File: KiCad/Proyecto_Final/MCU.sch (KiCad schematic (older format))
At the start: 74 parts

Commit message: Esquematico terminado con test points.
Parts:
- added J?: 5v, symbol Connector_Generic:Conn_01x02
- added J?: I2C1, symbol Connector_Generic:Conn_01x02
- added TP? (x34): TestPoint, symbol Connector:TestPoint
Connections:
- net +3.3VA: now also TP?.1
- net +3V3: now also TP?.1
- net ADC_22MHz: now also TP?.1
- net ADC_45MHz: now also TP?.1
- net Filt_Bypass: now also TP?.1
- net Filtro: now also TP?.1
- net GND: now also J?.2 (Pin_2), TP?.1
- net I2C1_SCL: now also J?.1 (Pin_1), TP?.1
- net I2C1_SDA: now also J?.2 (Pin_2), TP?.1
- net MCU_CLK: now also TP?.1
- net MIX_CLK: now also TP?.1
- net NRST: now also TP?.1
- net RXHP: now also TP?.1
- net Rx_Amp: now also TP?.1
- net Rx_Amp_Bypass: now also TP?.1
- net Rx_Amp_Pwr: now also TP?.1
- net Rx_Mix: now also TP?.1
- net Rx_Mix_Bypass: now also TP?.1
- net SPI1_CS0: now also TP?.1
- net SPI1_CS1: now also TP?.1
- net SPI1_MISO: now also TP?.1
- net SPI1_MOSI: now also TP?.1
- net SPI1_SCK: now also TP?.1
- net SPI4_CS: now also TP?.1
- net SPI4_MISO: now also TP?.1
- net SPI4_MOSI: now also TP?.1
- net SPI4_SCK: now also TP?.1
- net SWCLK: now also TP?.1
- net SWDIO: now also TP?.1
- net SWO: now also TP?.1
- net Trx_CLK: now also TP?.1
- net Trx_Enable: now also TP?.1
- net Trx_Rx_Enable: now also TP?.1
- net VBUS: now also J?.1 (Pin_1), TP?.1

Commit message: Primer hito presentado y visado.
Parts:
- FB?: value 220 @ 100MHz -> 120 @ 100MHz
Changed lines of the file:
@@
 P 1250 1300
 F 0 "FB?" V 976 1300 50  0000 C CNN
-F 1 "220 @ 100MHz" V 1067 1300 50  0000 C CNN
+F 1 "120 @ 100MHz" V 1067 1300 50  0000 C CNN
 F 2 "" V 1180 1300 50  0001 C CNN
 F 3 "~" H 1250 1300 50  0001 C CNN

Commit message: Empezando con el pcb, loquita.
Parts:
- C100, C101, C110, C89, C90, C94, C96, C99: renamed from C?; footprint (none) -> Capacitor_SMD:C_0805_2012Metric
- C102, C104, C105, C106, C107, C108, C109, C111, C76, C77, C78, C79, C80, C81, C82, C83, C84, C85, C86, C87, C88, C93, C95, C97, C98: renamed from C?; footprint (none) -> Capacitor_SMD:C_0402_1005Metric
- C103, C91, C92: renamed from C?; footprint (none) -> Capacitor_SMD:CP_Elec_4x5.4
- D2: renamed from D?; footprint (none) -> LED_SMD:LED_0603_1608Metric
- FB1, FB2, FB3: renamed from FB?; footprint (none) -> Inductor_SMD:L_0402_1005Metric
- J10, J8: renamed from J?; footprint (none) -> Connector_PinHeader_2.54mm:PinHeader_2x03_P2.54mm_Vertical_SMD
- J11, J12, J16: renamed from J?; footprint (none) -> Connector_PinHeader_2.54mm:PinHeader_2x04_P2.54mm_Vertical_SMD
- J13, J9: renamed from J?; footprint (none) -> Connector_PinHeader_2.54mm:PinHeader_2x06_P2.54mm_Vertical_SMD
- J14: renamed from J?; footprint (none) -> Connector_PinHeader_2.54mm:PinHeader_2x08_P2.54mm_Vertical_SMD
- J15: renamed from J?; footprint (none) -> Connector_PinHeader_2.54mm:PinHeader_1x04_P2.54mm_Vertical_SMD_Pin1Left
- J17, J3, J4: renamed from J?; footprint (none) -> Connector_PinHeader_2.54mm:PinHeader_2x01_P2.54mm_Vertical_SMD
- J5: renamed from J?; footprint (none) -> Connector_PinHeader_1.27mm:PinHeader_2x05_P1.27mm_Vertical_SMD
- J6: renamed from J?; footprint (none) -> Connector_USB:USB_Micro-B_Amphenol_10104110_Horizontal
- J7: renamed from J?; footprint (none) -> Connector_PinHeader_2.54mm:PinHeader_2x02_P2.54mm_Vertical_SMD
- R19: renamed from R?; footprint (none) -> Resistor_SMD:R_0402_1005Metric
- gave numbers to parts that had none: 54

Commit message: Empezado PCB.
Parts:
- added C112, C113: DNP, Capacitor_SMD:C_0402_1005Metric, symbol Device:C
- added R34, R35: 0, Resistor_SMD:R_0201_0603Metric, symbol Device:R
- added Y1: 25MHz, Crystal:Crystal_SMD_EuroQuartz_MT-4Pin_3.2x2.5mm, symbol Device:Crystal_GND24
- C103, C91, C92: footprint Capacitor_SMD:CP_Elec_4x5.4 -> Capacitor_SMD:C_0805_2012Metric
- J7: symbol Connector_Generic:Conn_02x02_Counter_Clockwise -> Connector_Generic:Conn_02x02_Odd_Even
- R20, R21, R22, R23, R24, R25, R26, R27, R28, R29, R30, R31, R32, R33: footprint (none) -> Resistor_SMD:R_0402_1005Metric
- SW1: footprint (none) -> SamacSys_Parts:PTS526SM15SMTR2LFS
- TP12, TP13, TP14, TP15, TP16, TP17, TP18, TP19, TP21, TP22, TP23, TP24, TP25, TP26, TP27, TP28, TP29, TP30, TP31, TP32, TP33, TP34, TP35, TP36, TP37, TP38, TP39, TP40, TP41, TP42, TP43, TP44, TP45: footprint (none) -> TestPoint:TestPoint_Pad_D1.0mm
- TP20: footprint (none) -> TestPoint:TestPoint_Pad_1.5x1.5mm
- U11: footprint (none) -> Package_TO_SOT_SMD:SOT-223-3_TabPin2
- U12: footprint DRY6 -> Tesis2020-21:TPD4S012DRYR
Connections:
- net +3V3: now also J7.2 (Pin_2); no longer J7.4 (Pin_4)
- net GND: now also J7.4 (Pin_4), C112.2, C113.2, Y1.2, Y1.4; no longer J7.3 (Pin_3)
- net at U14.3 (XOUT): now also R34.1
- net at U14.4 (XIN/REF): now also R35.1
- net at J7.1 (Pin_1), R24.1: now also J7.3 (Pin_3); no longer J7.2 (Pin_2)
- new net XIN: C113.1, R35.2, Y1.3
- new net XOUT: C112.1, R34.2, Y1.1
- no-connect marks 15 -> 13
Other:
- moved on the sheet: J17, R26, R27, R28, R29, R32, R33, TP31, TP32, TP33, TP34, TP35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

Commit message: Avance PCB.
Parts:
- J16: value CLK_SEL -> CFG_SEL
- renumbered R19 to R16, R20 to R17, R21 to R18, R22 to R19, R23 to R20, R24 to R21, R25 to R22, R34 to R23, R35 to R24, R26 to R25, R27 to R26, R28 to R27, R29 to R28, R30 to R29, R31 to R30, R32 to R31, R33 to R32

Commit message: PCB Frontend terminado y empezado parte Transceptor.
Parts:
- renumbered C101 to C100, C102 to C101, C103 to C102, C104 to C103, C105 to C104, C106 to C105, C107 to C106, C108 to C107, C109 to C108, C110 to C109, C111 to C110, C112 to C111, C113 to C112, C76 to C75, C77 to C76, C78 to C77, C79 to C78, C80 to C79, C81 to C80, C82 to C81, C83 to C82, C84 to C83, C85 to C84, C86 to C85, C87 to C86, C88 to C87, C89 to C88, C90 to C89, C91 to C90, C92 to C91, C93 to C92, C94 to C93, C95 to C94, C96 to C95, C97 to C96, C98 to C97, C99 to C98, C100 to C99

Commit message: PCB MCU empezado.
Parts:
- removed C94: 100nF, Capacitor_SMD:C_0402_1005Metric, symbol Device:C
- removed C95: 1uF, Capacitor_SMD:C_0805_2012Metric, symbol Device:C
- removed R23, R24: 0, Resistor_SMD:R_0201_0603Metric, symbol Device:R
- added J16: OutEn, Connector_PinHeader_2.54mm:PinHeader_2x02_P2.54mm_Vertical_SMD, symbol Connector_Generic:Conn_02x02_Odd_Even
- added R27: 10k, Resistor_SMD:R_0402_1005Metric, symbol Device:R
- C101: renamed from C103; value 0.1uF -> 100nF
- C102: renamed from C104; value 0.1uF -> 100nF
- C103: renamed from C105; value 0.1uF -> 100nF
- C104: renamed from C106; value 0.1uF -> 100nF
- C105: renamed from C107; value 0.1uF -> 100nF
- C106: renamed from C108; value 0.1uF -> 100nF
- C108: renamed from C110; value 0.1uF -> 100nF
- U14: value 5P49V6975 -> 5P49V5929
- renumbered C102 to C100, C109 to C107, C111 to C109, C112 to C110, C96 to C94, C97 to C95, C98 to C96, C99 to C97, C100 to C98, C101 to C99, J16 to J17, J17 to J18, R16 to R17, R17 to R18, R18 to R19, R19 to R20, R20 to R21, R21 to R22, R22 to R23, R25 to R24, R26 to R25, R27 to R26
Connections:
- net +3V3: now also J16.2 (Pin_2)
- net A_B: now also U13.56 (PG0); no longer U13.50 (PF12)
- net D0: now also U13.50 (PF12); no longer U13.53 (PF13)
- net D1: now also U13.53 (PF13); no longer U13.54 (PF14)
- net D2: now also U13.54 (PF14); no longer U13.55 (PF15)
- net D3: now also U13.55 (PF15); no longer U13.56 (PG0)
- net GND: now also J16.4 (Pin_4)
- net PD0: no longer U13.49 (PF11)
- net PD1: no longer U13.48 (PB2)
- net XIN: now also U14.4 (XIN/REF)
- net XOUT: now also U14.3 (XOUT)
- net SD_OE: now reaches U14.7 (SD/OE)
- net SD_OE: now also R27.2
- net USB_OTG_HS_DM renamed USB_OTG_HS_D-
- net USB_OTG_HS_DP renamed USB_OTG_HS_D+
- new net: J16.1 (Pin_1), J16.3 (Pin_3), R27.1
- new net PD0_adc: U13.48 (PB2)
- new net PD1_adc: U13.49 (PF11)

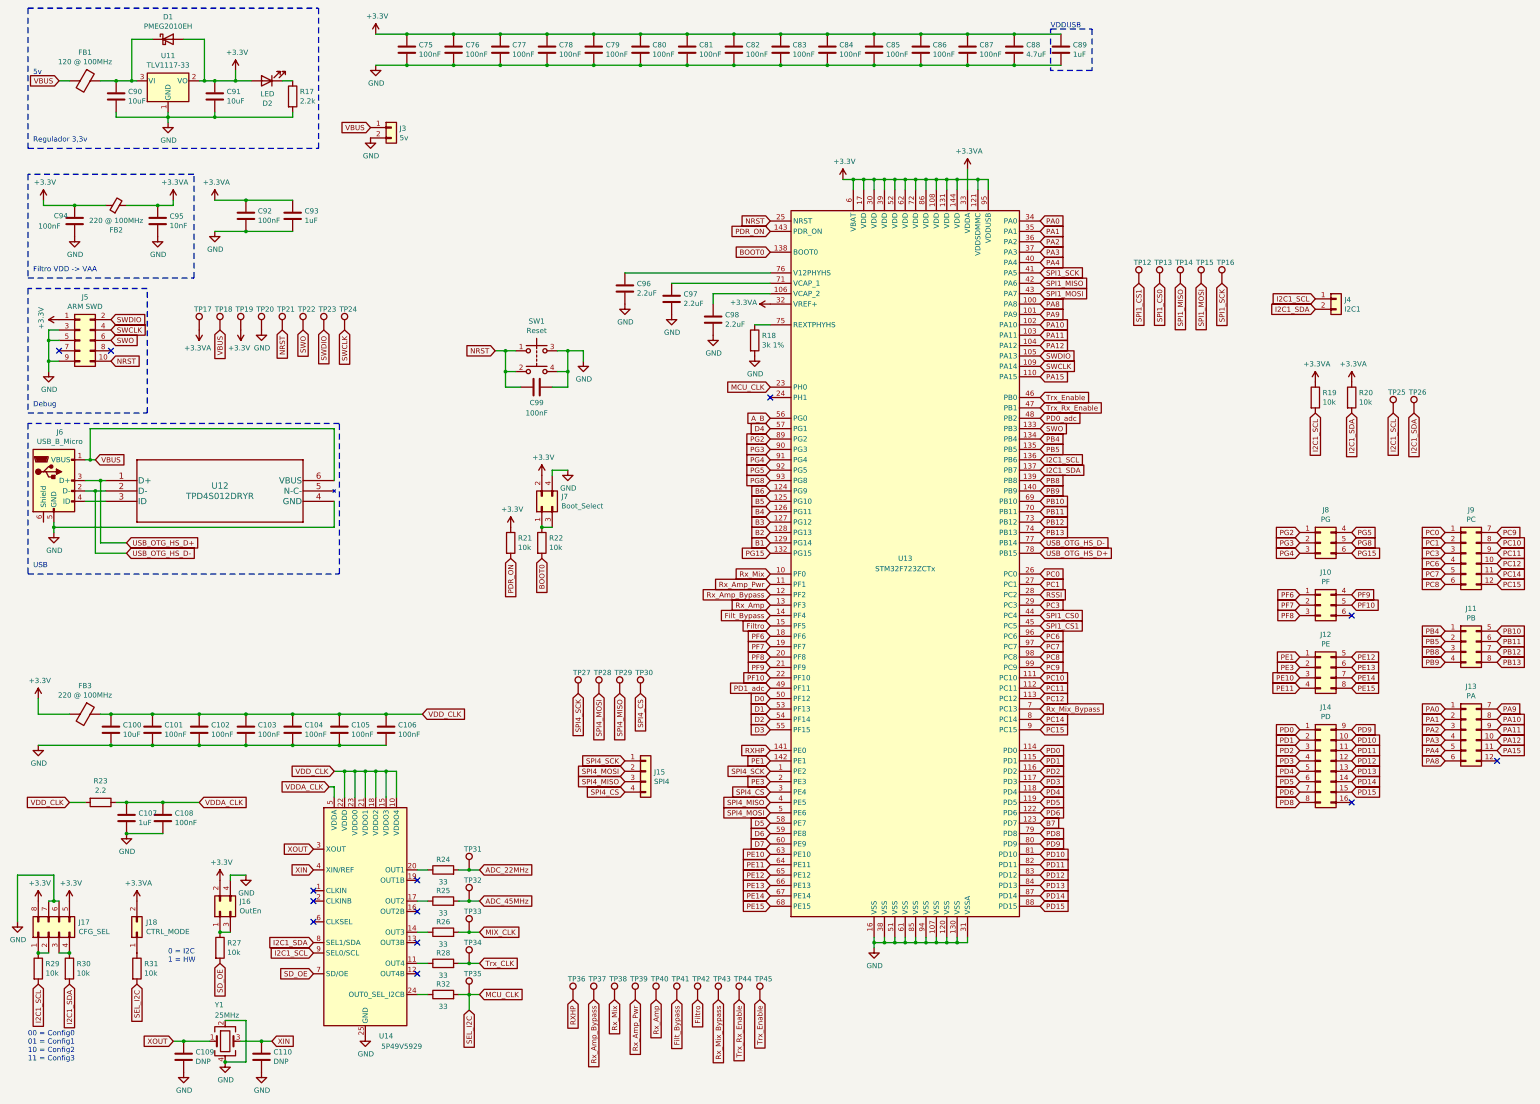
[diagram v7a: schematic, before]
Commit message: Reasignación de footprints por cambio de proveedor de componentes (JLCPCB SMT Assembly).
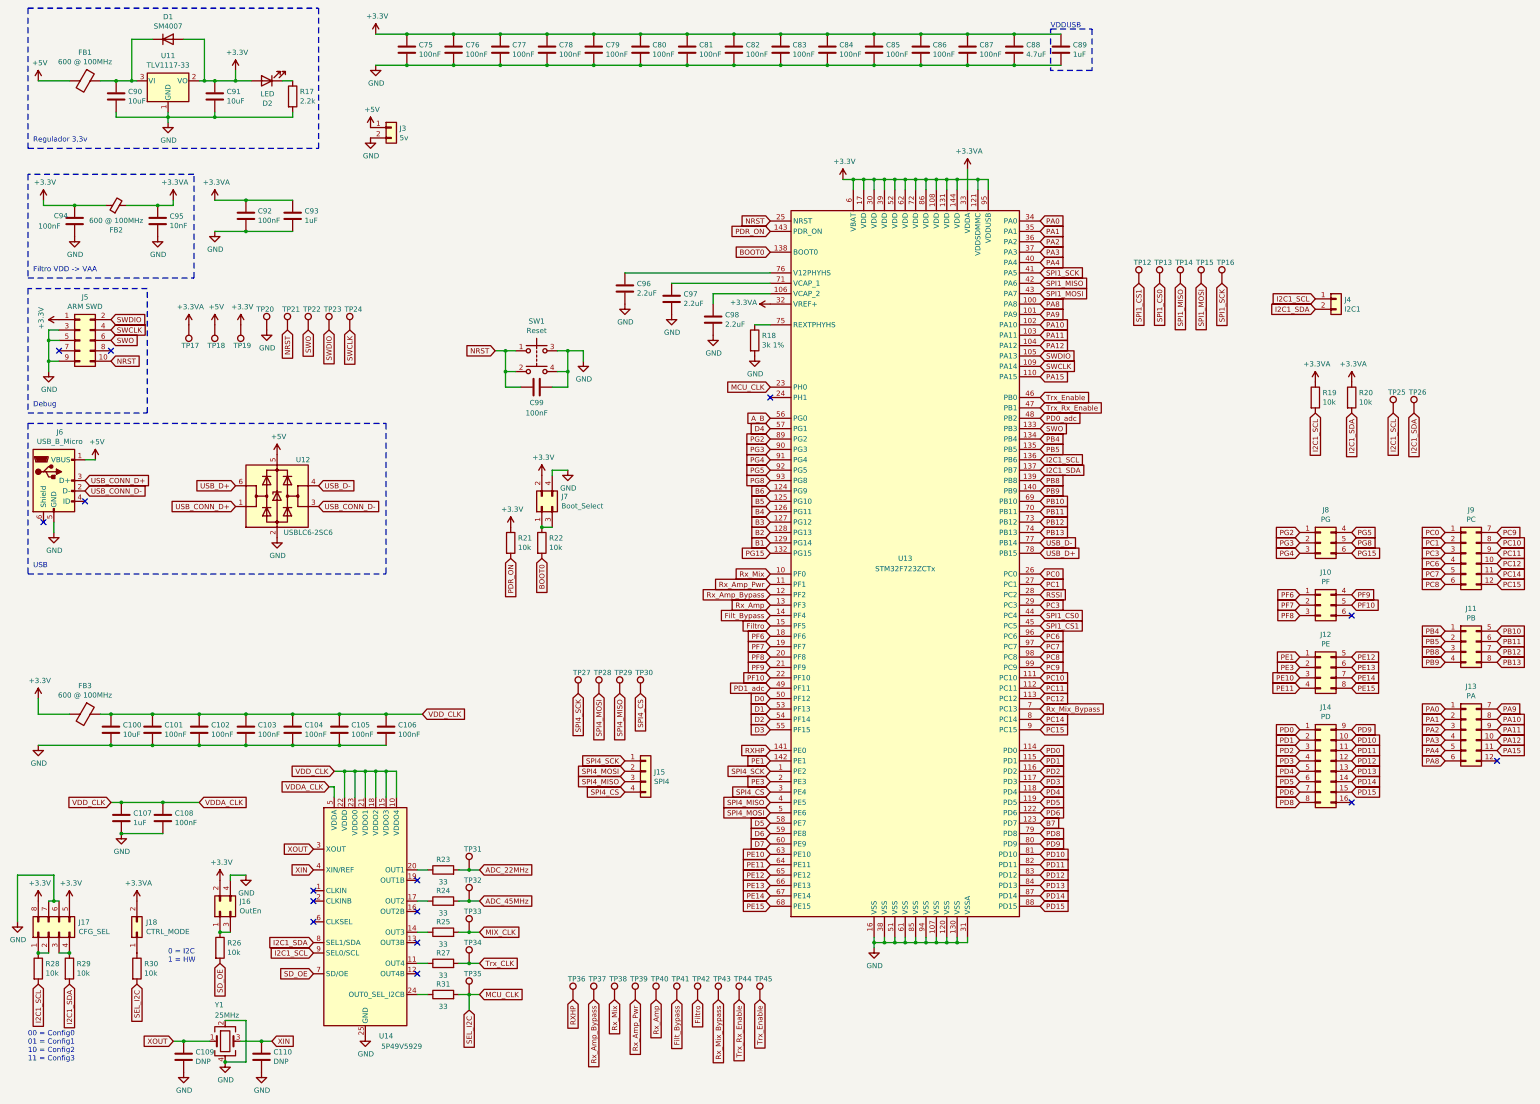
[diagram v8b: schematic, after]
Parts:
- removed D1: PMEG2010EH, Diode_SMD:D_SOD-123F, symbol Diode:PMEG2010EH
- removed R23: 2.2, Resistor_SMD:R_0402_1005Metric, symbol Device:R
- removed U12: TPD4S012DRYR, Tesis2020-21:TPD4S012DRYR, symbol TPD4S012DRYR:TPD4S012DRYR
- added D1: SM4007, Diode_SMD:D_SOD-123F, symbol Diode:SM4007
- added U12: USBLC6-2SC6, Package_TO_SOT_SMD:SOT-23-6, symbol Power_Protection:USBLC6-2SC6
- FB1: value 120 @ 100MHz -> 600 @ 100MHz
- FB2, FB3: value 220 @ 100MHz -> 600 @ 100MHz
- renumbered R24 to R23, R25 to R24, R26 to R25, R27 to R26, R28 to R27, R29 to R28, R30 to R29, R31 to R30, R32 to R31
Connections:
- net VDD_CLK is gone; now on net VDDA_CLK: C100.1, C101.1, C102.1, C103.1, C104.1, C105.1, C106.1, FB3.1, U14.10 (VDDO4), U14.15 (VDDO3), U14.18 (VDDO2), U14.21 (VDDO1), U14.22 (VDDD), U14.23 (VDDO0)
- net +3V3: now also D1.2 (A)
- net GND: now also U12.2 (GND)
- net at C90.1, FB1.1, U11.3 (VI): now also D1.1 (K)
- net USB_OTG_HS_D+ renamed USB_CONN_D+
- net USB_CONN_D+: now also U12.1 (I/O1); no longer U13.78 (PB15)
- net USB_OTG_HS_D- renamed USB_CONN_D-
- net USB_CONN_D-: now also U12.3 (I/O2); no longer U13.77 (PB14)
- net VBUS renamed +5V
- net +5V: now also U12.5 (VBUS)
- new net USB_D+: U12.6 (I/O1), U13.78 (PB15)
- new net USB_D-: U12.4 (I/O2), U13.77 (PB14)
- no-connect marks 13 -> 15
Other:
- note removed: "5v"
- moved on the sheet: C107, TP17, TP18, TP19, TP20, TP21, TP22, TP23, TP24
